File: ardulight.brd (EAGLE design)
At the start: 33 x 12.1 mm, 22 parts, among them U1 ATMEGA32U4QFN2, Y1 16MHz

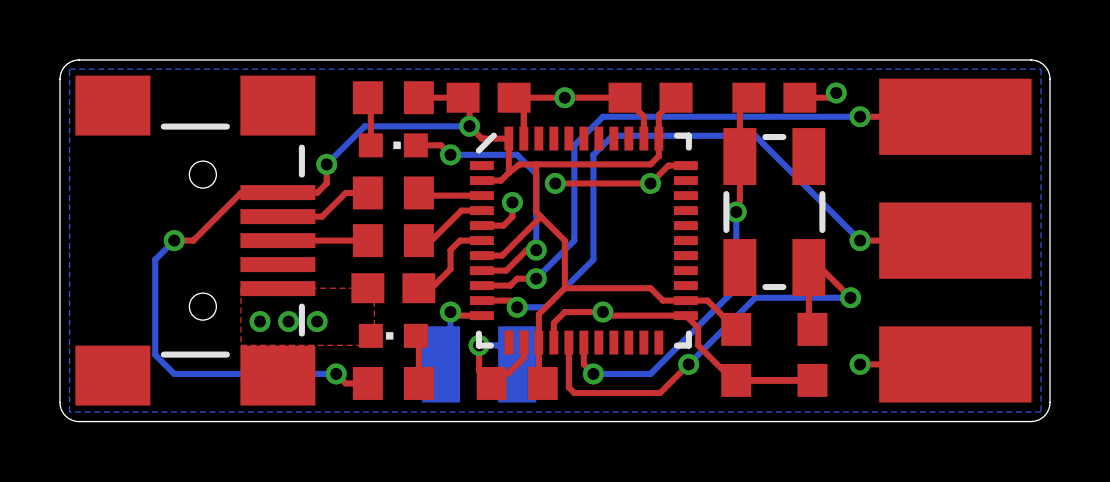
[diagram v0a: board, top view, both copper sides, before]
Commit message: add vcc to isp
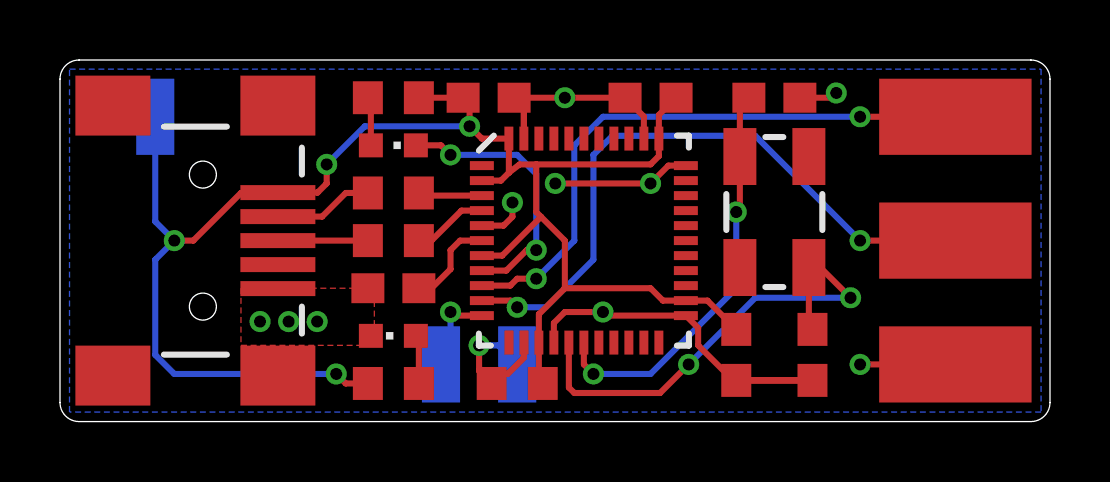
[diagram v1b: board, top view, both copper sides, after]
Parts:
- added VCC: (no value), wirepad:SMD1,27-2,54
- moved U$1 20.7 mm to (24.1, 2.22), turned to 0 degrees
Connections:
- net +5V: now also VCC.1
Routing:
- net +5V: track 53.8 -> 58.2 mm
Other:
- board text removed: "OpenSourceHW"
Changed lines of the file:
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@@
 <?xml version="1.0" encoding="utf-8"?>
 <!DOCTYPE eagle SYSTEM "eagle.dtd">
-<eagle version="6.4">
+<eagle version="6.5.0">
 <drawing>
 <settings>
@@
 <wire x1="17.78" y1="5.08" x2="17.78" y2="0" width="0.1016" layer="22" style="shortdash"/>
 <text x="14.9225" y="3.65125" size="1.016" layer="22" font="vector" rot="MR0">ISP</text>
-<text x="25.4" y="9.525" size="1.27" layer="22" font="vector" rot="MR0">Ardulight - Rev 1.0</text>
-<text x="25.4" y="7.62" size="1.27" layer="22" font="vector" rot="MR0">diy-electronics.net</text>
-<text x="0.9525" y="0.635" size="1.016" layer="22" font="vector" rot="MR90">OpenSourceHW</text>
+<text x="26.3525" y="9.2075" size="1.27" layer="22" font="vector" rot="MR0">Ardulight - Rev 1.0</text>
+<text x="26.3525" y="7.62" size="1.27" layer="22" font="vector" rot="MR0">diy-electronics.net</text>
 <wire x1="33.02" y1="8.89" x2="27.305" y2="8.89" width="0.1016" layer="22"/>
 <wire x1="27.305" y1="8.89" x2="27.305" y2="11.43" width="0.1016" layer="22"/>
@@
 <wire x1="27.305" y1="3.175" x2="27.305" y2="0.635" width="0.1016" layer="22"/>
 <wire x1="27.305" y1="0.635" x2="33.02" y2="0.635" width="0.1016" layer="22"/>
+<wire x1="2.2225" y1="12.065" x2="2.2225" y2="8.255" width="0.1016" layer="22" style="shortdash"/>
+<wire x1="2.2225" y1="8.255" x2="5.3975" y2="8.255" width="0.1016" layer="22" style="shortdash"/>
+<wire x1="5.3975" y1="8.255" x2="5.3975" y2="12.065" width="0.1016" layer="22" style="shortdash"/>
+<text x="1.74625" y="11.43" size="1.016" layer="22" font="vector" rot="MR270">ISP</text>
 </plain>
 <attributes>
@@
 <attribute name="NAME" x="10.6425" y="0.775" size="1.016" layer="26" font="vector" rot="MR90"/>
 </element>
-<element name="U$1" library="SparkFun-Aesthetics" package="OSHW-LOGO-S" value="" x="3.81" y="6.0325" rot="MR90"/>
+<element name="U$1" library="SparkFun-Aesthetics" package="OSHW-LOGO-S" value="" x="24.13" y="2.2225" rot="MR0"/>
+<element name="VCC" library="wirepad" package="SMD1,27-2,54" value="" x="3.175" y="10.16" smashed="yes" rot="MR180">
+<attribute name="VALUE" x="3.175" y="10.16" size="0.0254" layer="28" rot="MR180"/>
+<attribute name="NAME" x="4.13375" y="8.87125" size="1.016" layer="22" font="vector" rot="MR90"/>
+</element>
 </elements>
 <signals>
@@
 <wire x1="6.0325" y1="7.62" x2="7.25" y2="7.62" width="0.2032" layer="1"/>
 <wire x1="7.25" y1="7.62" x2="7.2625" y2="7.6325" width="0.2032" layer="1"/>
+<contactref element="VCC" pad="1"/>
+<wire x1="3.175" y1="10.16" x2="3.175" y2="6.6675" width="0.2032" layer="16"/>
+<wire x1="3.175" y1="6.6675" x2="3.81" y2="6.0325" width="0.2032" layer="16"/>
 </signal>
 <signal name="RST">

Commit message: more information regarding assembly etc
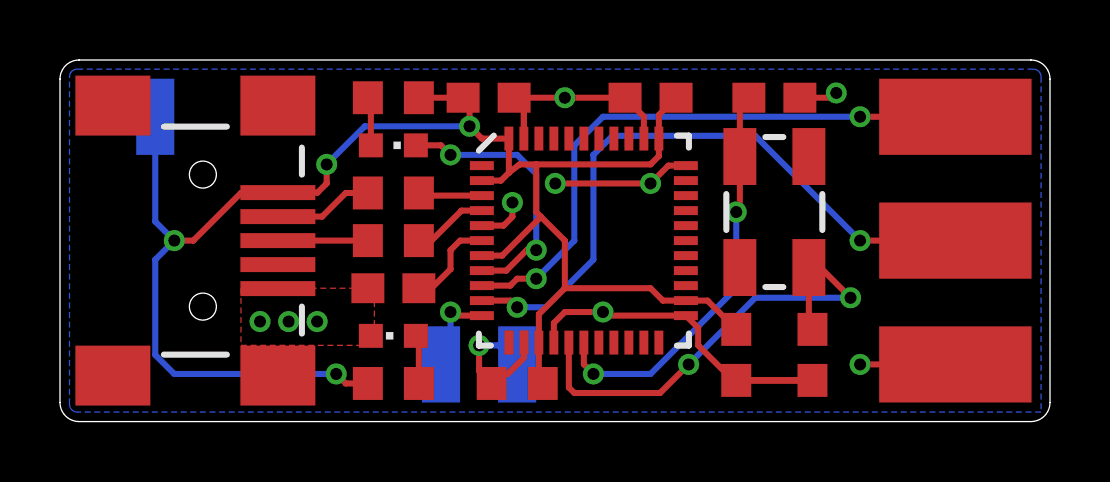
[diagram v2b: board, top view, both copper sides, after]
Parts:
- PWR: value (none) -> BLUE
- R1: value 1k -> 82R
- R5: value 1k -> 150R
- RX: value (none) -> YLW
